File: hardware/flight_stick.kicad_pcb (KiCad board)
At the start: 2 copper layers, 75 x 50 mm, 61 parts, among them J1 Load Cell 1, J10 USB_C_Receptacle_USB2.0, J11 Conn_01x05_Pin, J3 Load Cell 2, J5 Load Cell 3, J7 Conn_01x04_Male, J8 Conn_01x05_Pin, J9 Conn_ST_STDC14, Q4 2N7002, Q5 2N7002, Q6 2N7002, Q7 2N7002, Q8 2N7002, SW1 KMR223G LFG, U1 ADS131M03IRUKx, U2 LM3940IMP-3.3/NOPB, U4 STM32F103CBU6, Y1 8M

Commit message: Finished footprint assignment and deleted pcb
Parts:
- removed C1, C16, C17, C18, C19, C2, C3, C5, C6: 100n, Capacitor_SMD:C_0603_1608Metric
- removed C20: 470n, Capacitor_SMD:C_0603_1608Metric
- removed C4: 220n, Capacitor_SMD:C_0603_1608Metric
- removed C7, C8, C9: 10u, Capacitor_SMD:C_0603_1608Metric
- removed D1, D2, D3: LED, LED_SMD:LED_0805_2012Metric
- removed D4: SMLVN6RGB, LED_SMD:LED_ROHM_SMLVN6
- removed H1, H2, H3: MountingHole, MountingHole:MountingHole_3.2mm_M3_ISO7380
- removed J1: Load Cell 1, Connector_PinHeader_1.27mm:PinHeader_1x04_P1.27mm_Vertical
- removed J10: USB_C_Receptacle_USB2.0, Connector_USB:USB_C_Receptacle_HRO_TYPE-C-31-M-12
- removed J11, J8: Conn_01x05_Pin, Connector_PinHeader_2.54mm:PinHeader_1x05_P2.54mm_Vertical
- removed J3: Load Cell 2, Connector_PinHeader_1.27mm:PinHeader_1x04_P1.27mm_Vertical
- removed J5: Load Cell 3, Connector_PinHeader_1.27mm:PinHeader_1x04_P1.27mm_Vertical
- removed J7: Conn_01x04_Male, Connector_JST:JST_XH_B4B-XH-A_1x04_P2.50mm_Vertical
- removed J9: Conn_ST_STDC14, Connector_PinHeader_1.27mm:PinHeader_2x07_P1.27mm_Vertical_SMD
- removed Q4, Q5, Q6, Q7, Q8: 2N7002, Package_TO_SOT_SMD:SOT-23
- removed R1, R2, R3, R4, R5, R6: 1k, Resistor_SMD:R_0603_1608Metric
- removed R10, R8: 50, Resistor_SMD:R_0603_1608Metric
- removed R20, R25, R26, R27, R28, R29: 10k, Resistor_SMD:R_0603_1608Metric
- removed R21, R22: 22, Resistor_SMD:R_0603_1608Metric
- removed R23, R24: 5.1K, Resistor_SMD:R_0603_1608Metric
- removed R30: 200, Resistor_SMD:R_0603_1608Metric
- removed R31: 300, Resistor_SMD:R_0603_1608Metric
- removed R7, R9: 100, Resistor_SMD:R_0603_1608Metric
- removed SW1: KMR223G LFG, flight_stick_footprints:KMR2_G_CNK
- removed U1: ADS131M03IRUKx, flight_stick_footprints:QFN_WQFN_RUK_TEX
- removed U2: LM3940IMP-3.3/NOPB, flight_stick_footprints:MP04A
- removed U4: STM32F103CBU6, Package_DFN_QFN:QFN-48-1EP_7x7mm_P0.5mm_EP5.6x5.6mm
- removed Y1: 8M, Crystal:Resonator_SMD_Murata_CSTxExxV-3Pin_3.0x1.1mm
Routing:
- net GND: track 301.4 -> 0.00 mm, vias 13 -> 0
- net +3.3V: track 190.1 -> 0.00 mm, vias 11 -> 0
- net +5V: track 102.4 -> 0.00 mm, vias 3 -> 0
- net /Trans5: track 53.9 -> 0.00 mm, vias 4 -> 0
- net /SCL: track 44.0 -> 0.00 mm
- net /SDA: track 41.7 -> 0.00 mm
- net /Trans4: track 41.1 -> 0.00 mm, vias 2 -> 0
- net /codeio: track 39.9 -> 0.00 mm, vias 4 -> 0
- net /mcureset: track 39.2 -> 0.00 mm, vias 4 -> 0
- net /Trans3: track 36.0 -> 0.00 mm, vias 2 -> 0
- net /button3: track 35.8 -> 0.00 mm, vias 1 -> 0
- net /ADC_CS: track 32.9 -> 0.00 mm, vias 2 -> 0
- net Net-(U4-PA7): track 32.5 -> 0.00 mm
- net /ADC_MCK: track 32.3 -> 0.00 mm, vias 2 -> 0
- net /ADC_SDO: track 29.7 -> 0.00 mm, vias 2 -> 0
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- removed copper zone on F.Cu, net GND
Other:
- board outline removed
- board text removed: "+"
- board text removed: "-"
- board text removed: "1 2 3 4 5"
- board text removed: "3V3"
- board text removed: "5 4 3 2 1"
- board text removed: "5V"
- board text removed: "A+"
- board text removed: "A-"
- board text removed: "Aryan Ghosh ^_^"
- board text removed: "CL"
- board text removed: "DA"
- board text removed: "University of Toronto Human Powered Vehicles Design Team"

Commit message: Began layout placement
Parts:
- added C1: 2.2u, Capacitor_SMD:C_0603_1608Metric, F.Cu at (42.2, 48.7)
- added C11: 100n, Capacitor_SMD:C_0603_1608Metric, F.Cu at (97.3, 58.7)
- added C12: 100n, Capacitor_SMD:C_0603_1608Metric, F.Cu at (97.3, 61.2)
- added C13: 220n, Capacitor_SMD:C_0603_1608Metric, F.Cu at (101.3, 53.7)
- added C14: 100n, Capacitor_SMD:C_0603_1608Metric, F.Cu at (101.3, 56.2)
- added C16: 100n, Capacitor_SMD:C_0603_1608Metric, F.Cu at (103.0, 81.0)
- added C17: 100n, Capacitor_SMD:C_0603_1608Metric, F.Cu at (103.8, 73.6)
- added C18: 100n, Capacitor_SMD:C_0603_1608Metric, F.Cu at (93.5, 81.0)
- added C19: 100n, Capacitor_SMD:C_0603_1608Metric, F.Cu at (97.0, 71.6)
- added C2: 22u, Capacitor_SMD:C_0603_1608Metric, F.Cu at (42.2, 51.2)
- added C23: 1u, Capacitor_SMD:C_0402_1005Metric, F.Cu at (11.5, 61.1)
- added C8: 100n, Capacitor_SMD:C_0603_1608Metric, F.Cu at (97.3, 53.7)
- added C9: 100n, Capacitor_SMD:C_0603_1608Metric, F.Cu at (97.3, 56.2)
- added D1: GREEN_LED, LED_SMD:LED_0805_2012Metric, F.Cu at (50.9, 58.0)
- added D10: D, Diode_SMD:D_SOD-123, F.Cu at (-1.49, 28.7)
- added D11: D, Diode_SMD:D_SOD-123, F.Cu at (-1.49, 32.0)
- added D12: D, Diode_SMD:D_SOD-123, F.Cu at (-1.49, 35.4)
- added D13: D, Diode_SMD:D_SOD-123, F.Cu at (4.30, 15.3)
- added D14: D, Diode_SMD:D_SOD-123, F.Cu at (4.30, 18.6)
- added D15: D, Diode_SMD:D_SOD-123, F.Cu at (4.30, 22.0)
- added D16: D, Diode_SMD:D_SOD-123, F.Cu at (4.30, 25.3)
- added D17: D, Diode_SMD:D_SOD-123, F.Cu at (4.30, 28.7)
- added D18: D, Diode_SMD:D_SOD-123, F.Cu at (4.30, 32.0)
- added D19: D, Diode_SMD:D_SOD-123, F.Cu at (4.30, 35.4)
- added D20: D, Diode_SMD:D_SOD-123, F.Cu at (10.1, 15.3)
- added D21: D, Diode_SMD:D_SOD-123, F.Cu at (10.1, 18.6)
- added D22: D, Diode_SMD:D_SOD-123, F.Cu at (10.1, 22.0)
- added D23: D, Diode_SMD:D_SOD-123, F.Cu at (10.1, 25.3)
- added D24: D, Diode_SMD:D_SOD-123, F.Cu at (10.1, 28.7)
- added D25: D, Diode_SMD:D_SOD-123, F.Cu at (10.1, 32.0)
- added D26: D, Diode_SMD:D_SOD-123, F.Cu at (10.1, 35.4)
- added D27: D, Diode_SMD:D_SOD-123, F.Cu at (15.9, 15.3)
- added D28: D, Diode_SMD:D_SOD-123, F.Cu at (15.9, 18.6)
- added D29: D, Diode_SMD:D_SOD-123, F.Cu at (15.9, 22.0)
- added D3: D, Diode_SMD:D_SOD-123, F.Cu at (-1.49, 15.3)
- added D30: D, Diode_SMD:D_SOD-123, F.Cu at (15.9, 25.3)
- added D4: SMLVN6RGB, LED_SMD:LED_ROHM_SMLVN6, F.Cu at (33.5, 43.0)
- added D5: D, Diode_SMD:D_SOD-123, F.Cu at (-1.49, 18.6)
- added D6: SS34, Diode_SMD:D_SMA, F.Cu at (48.2, 49.7)
- added D7: SS34, Diode_SMD:D_SMA, F.Cu at (48.2, 54.2)
- added D8: D, Diode_SMD:D_SOD-123, F.Cu at (-1.49, 22.0)
- added D9: D, Diode_SMD:D_SOD-123, F.Cu at (-1.49, 25.3)
- added J1: Conn_01x04_Male, Connector_JST:JST_XH_B4B-XH-A_1x04_P2.50mm_Vertical, F.Cu at (-0.94, 58.9)
- added J10: USB_C_Receptacle_USB2.0, Connector_USB:USB_C_Receptacle_HRO_TYPE-C-31-M-12, F.Cu at (105.8, 91.5)
- added J12: Load Cell 2, Connector_PinHeader_1.27mm:PinHeader_1x04_P1.27mm_Vertical, F.Cu at (105.7, 47.0)
- added J2: Conn_02x05_Top_Bottom, Connector_JST:JST_J2100_B10B-J21DK-GGXR_2x05_P2.50x4.00mm_Vertical, F.Cu at (24.9, 19.1)
- added J3: Conn_01x04_Male, Connector_JST:JST_XH_B4B-XH-A_1x04_P2.50mm_Vertical, F.Cu at (-0.94, 66.7)
- added J4: Load Cell 3, Connector_PinHeader_1.27mm:PinHeader_1x04_P1.27mm_Vertical, F.Cu at (97.3, 47.0)
- added J6: Load Cell 1, Connector_PinHeader_1.27mm:PinHeader_1x04_P1.27mm_Vertical, F.Cu at (101.5, 47.0)
- added J7: Conn_02x05_Top_Bottom, Connector_JST:JST_J2100_B10B-J21DK-GGXR_2x05_P2.50x4.00mm_Vertical, F.Cu at (-0.25, 42.5)
- added J9: Conn_ST_STDC14, Connector_PinHeader_1.27mm:PinHeader_2x07_P1.27mm_Vertical_SMD, F.Cu at (85.0, 84.3)
- added L2: 10uH, Inductor_SMD:L_0603_1608Metric, F.Cu at (42.2, 53.7)
- added R1: 10k, Resistor_SMD:R_0603_1608Metric, F.Cu at (42.2, 56.2)
- added R10: 200, Resistor_SMD:R_0603_1608Metric, F.Cu at (44.6, 24.9)
- added R12: 1k, Resistor_SMD:R_0603_1608Metric, F.Cu at (101.3, 58.7)
- added R13: 1k, Resistor_SMD:R_0603_1608Metric, F.Cu at (101.3, 61.2)
- added R14: 1k, Resistor_SMD:R_0603_1608Metric, F.Cu at (105.3, 53.7)
- added R15: 1k, Resistor_SMD:R_0603_1608Metric, F.Cu at (105.3, 56.2)
- added R16: 1k, Resistor_SMD:R_0603_1608Metric, F.Cu at (105.3, 58.7)
- added R17: 1k, Resistor_SMD:R_0603_1608Metric, F.Cu at (105.3, 61.2)
- added R2: 4.7k, Resistor_SMD:R_0603_1608Metric, F.Cu at (108.3, 72.9)
- added R20: 10k, Resistor_SMD:R_0603_1608Metric, F.Cu at (97.0, 70.0)
- added R23: 5.1K, Resistor_SMD:R_0603_1608Metric, F.Cu at (99.5, 88.5)
- added R24: 5.1K, Resistor_SMD:R_0603_1608Metric, F.Cu at (112.5, 88.5)
- added R3: 4.7k, Resistor_SMD:R_0603_1608Metric, F.Cu at (112.3, 62.9)
- added R30: 10k, Resistor_SMD:R_0603_1608Metric, F.Cu at (15.4, 40.8)
- added R31: 10k, Resistor_SMD:R_0603_1608Metric, F.Cu at (15.4, 43.3)
- added R32: 10k, Resistor_SMD:R_0603_1608Metric, F.Cu at (15.4, 45.8)
- added R33: 10k, Resistor_SMD:R_0603_1608Metric, F.Cu at (15.4, 48.3)
- added R4: 400, Resistor_SMD:R_0603_1608Metric, F.Cu at (42.2, 58.7)
- added R5: 10k, Resistor_SMD:R_0603_1608Metric, F.Cu at (15.4, 38.3)
- added R7: 1.5k, Resistor_SMD:R_0603_1608Metric, F.Cu at (106.5, 83.8)
- added R8: 200, Resistor_SMD:R_0603_1608Metric, F.Cu at (44.6, 19.9)
- added R9: 200, Resistor_SMD:R_0603_1608Metric, F.Cu at (44.6, 22.4)
- added SW1: KMR223G LFG, flight_stick_footprints:KMR2_G_CNK, F.Cu at (93.0, 69.5)
- added U1: TPS62175DQC, Package_SON:WSON-10-1EP_2x3mm_P0.5mm_EP0.84x2.4mm_ThermalVias, F.Cu at (46.5, 58.8)
- added U2: AT24CS01-MAHM, Package_DFN_QFN:DFN-8-1EP_3x2mm_P0.5mm_EP1.3x1.5mm, F.Cu at (109.2, 76.1)
- added U3: ADS131M03IRUKx, flight_stick_footprints:QFN_WQFN_RUK_TEX, F.Cu at (35.5, 57.4)
- added U4: STM32F103CBU6, Package_DFN_QFN:QFN-48-1EP_7x7mm_P0.5mm_EP5.6x5.6mm, F.Cu at (98.5, 76.5)
- added U5: USBLC6-2SC6, Package_TO_SOT_SMD:SOT-23-6, F.Cu at (100.0, 84.0)
- added U6: TCAN3403, Package_TO_SOT_SMD:TSOT-23-8, F.Cu at (12.6, 57.9)
- added Y1: 8M, Crystal:Resonator_SMD_Murata_CSTxExxV-3Pin_3.0x1.1mm, F.Cu at (100.8, 70.6)

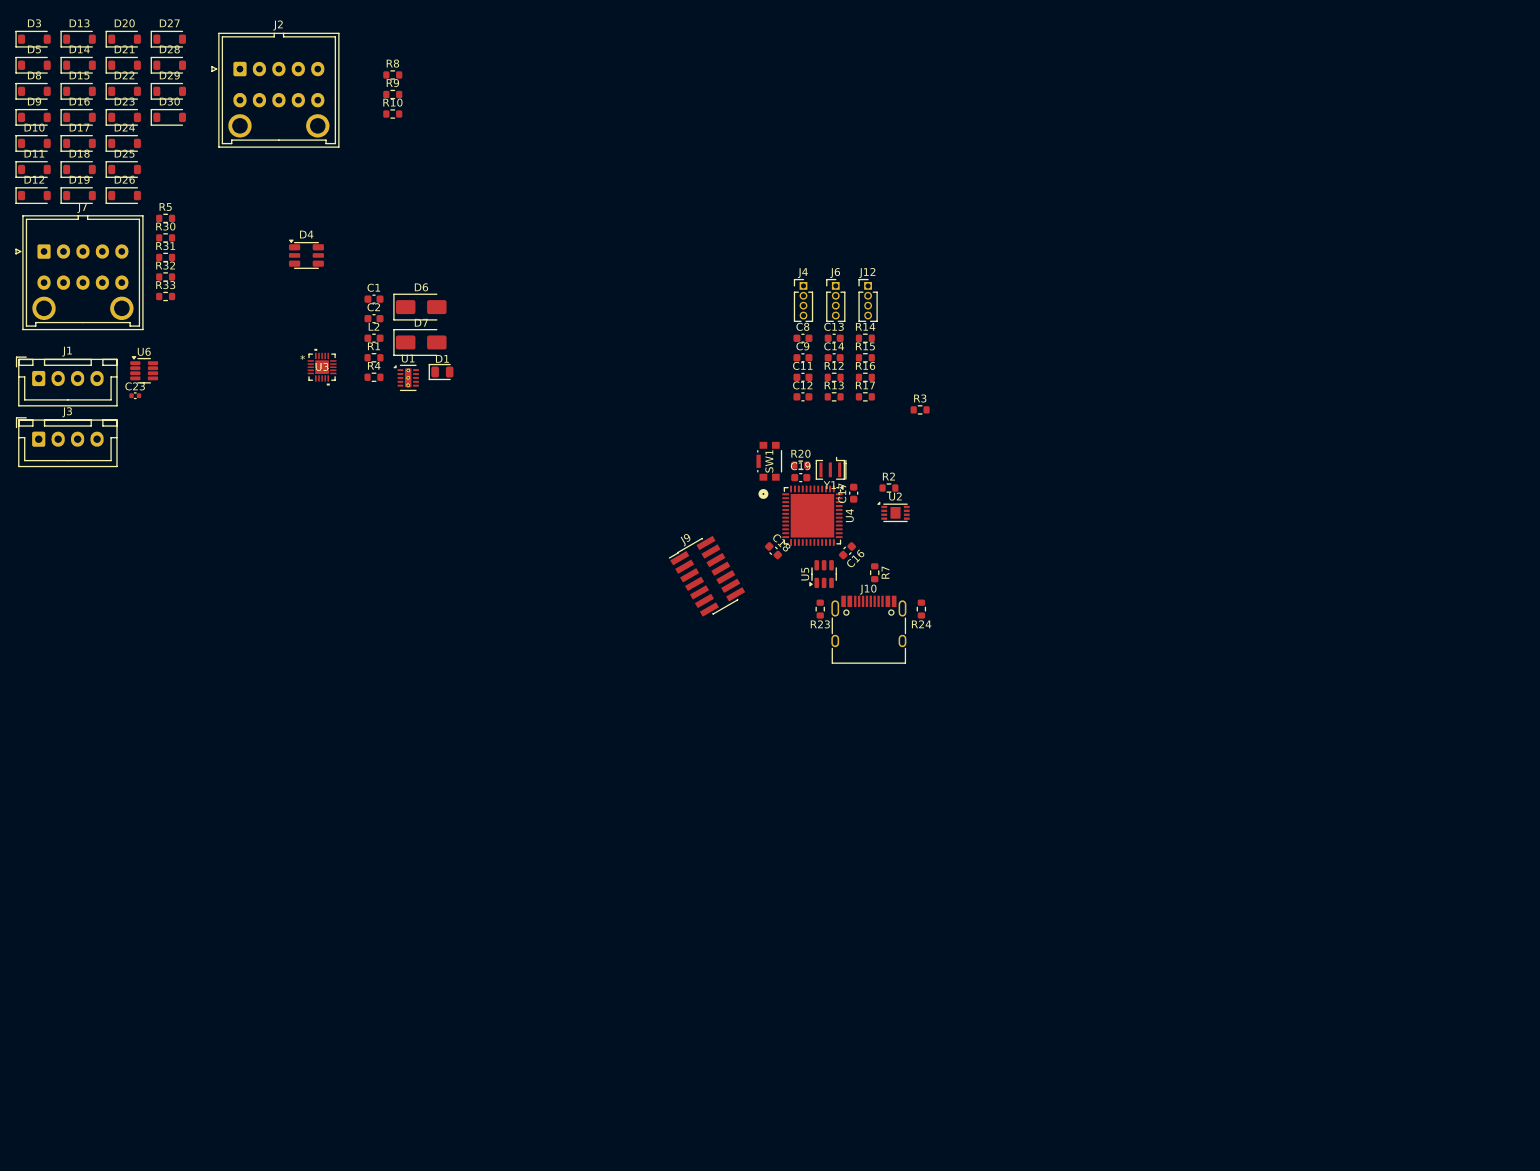
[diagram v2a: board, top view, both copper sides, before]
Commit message: modified mcu pin alloc and pre-routing placement
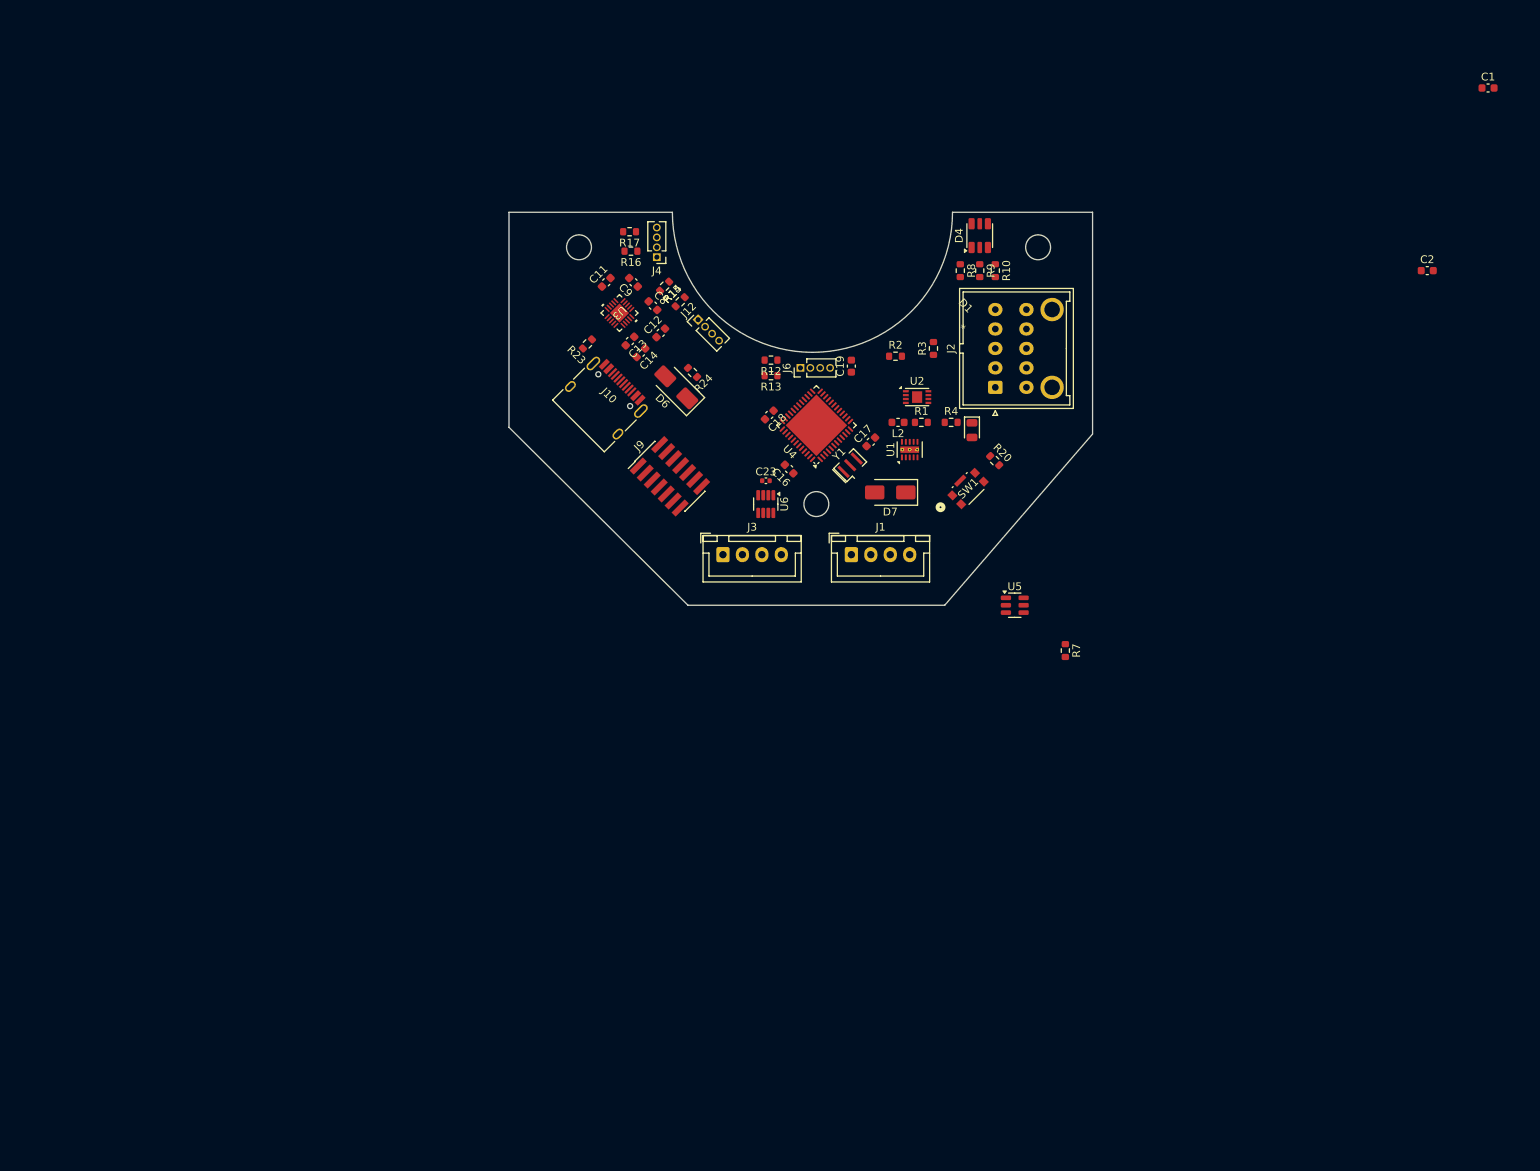
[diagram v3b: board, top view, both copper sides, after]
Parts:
- removed D10, D11, D12, D13, D14, D15, D16, D17, D18, D19, D20, D21, D22, D23, D24, D25, D26, D27, D28, D29, D3, D30, D5, D8, D9: D, Diode_SMD:D_SOD-123
- removed J7: Conn_02x05_Top_Bottom, Connector_JST:JST_J2100_B10B-J21DK-GGXR_2x05_P2.50x4.00mm_Vertical
- removed R30, R31, R32, R33, R5: 10k, Resistor_SMD:R_0603_1608Metric
- added H1: MountingHole, MountingHole:MountingHole_3.2mm_M3, F.Cu at (68.5, 42.0)
- added H2: MountingHole, MountingHole:MountingHole_3.2mm_M3, F.Cu at (127.5, 42.0)
- added H3: MountingHole, MountingHole:MountingHole_3.2mm_M3, F.Cu at (99.0, 75.0)
- moved C1 145.7 mm to (185.3, 21.5)
- moved C2 135.5 mm to (177.5, 45.0)
- moved J1 106.9 mm to (103.5, 81.5)
- moved J2 105.3 mm to (122.0, 60.0), turned to 90 degrees
- moved J3 89.2 mm to (87.0, 81.5)
- moved D4 86.6 mm to (120.0, 40.5), turned to 90 degrees
- moved C23 81.8 mm to (92.5, 72.0)
- moved U6 81.7 mm to (92.5, 75.0), turned to -90 degrees
- moved R10 80.0 mm to (122.0, 45.0), turned to -90 degrees
- moved R9 78.8 mm to (120.0, 45.0), turned to -90 degrees
- moved R8 77.1 mm to (117.5, 45.0), turned to -90 degrees
- moved R4 74.4 mm to (116.3, 64.5)
- moved R1 70.8 mm to (112.5, 64.5)
- moved D1 68.5 mm to (119.0, 65.5), turned to -90 degrees
- moved L2 68.2 mm to (109.5, 64.5), turned to 180 degrees
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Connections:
- U4 pad 12: /COMPRT_TX -> /MTX_COL2
- U4 pad 13: /COMPRT_RX -> /MTX_COL3
- U4 pad 14: /MTX_COL2 -> /MTX_COL4
- U4 pad 15: /MTX_COL3 -> /MTX_COL5
- U4 pad 16: /MTX_COL4 -> /MTX_ROW1
- U4 pad 17: /MTX_COL5 -> /MTX_ROW2
- U4 pad 18: /MTX_ROW1 -> /MTX_ROW3
- U4 pad 19: /MTX_ROW2 -> /MTX_ROW4
- U4 pad 20: /MTX_ROW3 -> /MTX_ROW5
- U4 pad 21: /MTX_ROW4 -> /ADC_CS
- U4 pad 22: /MTX_ROW5 -> /ADC_RST
- U4 pad 30: /ADC_CS -> /COMPRT_TX
- U4 pad 31: /ADC_RST -> /COMPRT_RX
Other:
- board outline added: 75 x 50.5 mm
- board text added: "1 in. Shaft Outer Diameter"

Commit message: Completed first layout draft
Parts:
- added C3: 2.2u, Capacitor_SMD:C_0603_1608Metric, F.Cu at (102.0, 86.5)
- added NT1: NetTie_2, NetTie:NetTie-2_THT_Pad1.0mm, F.Cu at (71.5, 57.7)
- J2: value Conn_02x05_Top_Bottom -> Conn_02x05_Odd_Even; footprint Connector_JST:JST_J2100_B10B-J21DK-GGXR_2x05_P2.50x4.00mm_Vertical -> Connector_JST:JST_PUD_B10B-PUDSS_2x05_P2.00mm_Vertical
- R1: value 10k -> 100k
- moved C1 110.9 mm to (95.5, 86.5), turned to 90 degrees
- moved C2 84.1 mm to (102.0, 82.0), turned to -90 degrees
- moved R7 60.1 mm to (77.0, 67.5), turned to 135 degrees
- moved U5 47.2 mm to (82.5, 66.5)
- moved R20 38.7 mm to (85.5, 82.5)
- moved SW1 37.5 mm to (83.0, 85.0), turned to -45 degrees
- moved D6 28.2 mm to (90.5, 86.5), turned to 180 degrees
- moved J3 27.7 mm to (114.7, 82.8), turned to 45 degrees
- moved J1 23.9 mm to (125.5, 72.0), turned to 45 degrees
- moved L2 22.8 mm to (95.5, 82.5), turned to -90 degrees
- moved R1 22.0 mm to (98.5, 81.5)
- moved U1 20.8 mm to (99.0, 85.0)
- moved U6 20.0 mm to (112.5, 76.0), turned to -45 degrees
- moved D1 19.4 mm to (108.0, 81.5), turned to 180 degrees
- moved R4 18.7 mm to (104.5, 79.0)
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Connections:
- net Net-(U4-PD0) renamed /OSC+
- net Net-(U4-PD1) renamed /OSC-
- C12 pad 2: GND -> GNDA
- J12 pad 4: GND -> GNDA
- J2 pad 2: /MTX_ROW2 -> /MTX_COL1
- J2 pad 3: /MTX_ROW3 -> /MTX_ROW2
- J2 pad 4: /MTX_ROW4 -> /MTX_COL2
- J2 pad 5: /MTX_ROW5 -> /MTX_ROW3
- J2 pad 6: /MTX_COL1 -> /MTX_COL3
- J2 pad 7: /MTX_COL2 -> /MTX_ROW4
- J2 pad 8: /MTX_COL3 -> /MTX_COL4
- J2 pad 9: /MTX_COL4 -> /MTX_ROW5
- J4 pad 4: GND -> GNDA
- J6 pad 4: GND -> GNDA
- R4 pad 1: /Power/PG -> +3.3V
- U3 pad 20: GND -> GNDA
- U3 pad 21: GND -> GNDA
- U4 pad 11: /MTX_COL1 -> /MTX_COL5
- U4 pad 12: /MTX_COL2 -> /MTX_COL4
- U4 pad 14: /MTX_COL4 -> /MTX_COL2
- U4 pad 15: /MTX_COL5 -> /MTX_COL1
- U4 pad 21: /ADC_CS -> /EEPROM_SCK
- U4 pad 22: /ADC_RST -> /EEPROM_SDA
- U4 pad 30: /COMPRT_TX -> /ADC_CS
- U4 pad 31: /COMPRT_RX -> /ADC_RST
- U4 pad 42: /EEPROM_SCK -> /COMPRT_TX
- U4 pad 43: /EEPROM_SDA -> /COMPRT_RX
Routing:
- net GND: track 0.00 -> 175.7 mm, vias 0 -> 8
- net +3.3V: track 0.00 -> 102.9 mm, vias 0 -> 9
- net +5V: track 0.00 -> 60.1 mm, vias 0 -> 2
- net /RESET: track 0.00 -> 55.7 mm, vias 0 -> 3
- net /MTX_COL5: track 0.00 -> 45.0 mm
- net /MTX_COL4: track 0.00 -> 41.5 mm
- net /RGB_B: track 0.00 -> 40.9 mm, vias 0 -> 2
- net /RGB_G: track 0.00 -> 39.3 mm, vias 0 -> 2
- net /RGB_R: track 0.00 -> 39.2 mm, vias 0 -> 2
- net /MTX_COL3: track 0.00 -> 38.3 mm
- net /MTX_COL2: track 0.00 -> 35.8 mm
- net /MTX_ROW5: track 0.00 -> 34.8 mm
- net /ADC_DRDY: track 0.00 -> 34.3 mm, vias 0 -> 2
- net /MTX_ROW4: track 0.00 -> 33.8 mm
- net /MTX_ROW3: track 0.00 -> 32.8 mm
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- added copper zone on In1.Cu, net +3.3V
- added copper zone on In2.Cu, net GND
- added copper zone on In2.Cu, net GNDA
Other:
- board size 75 x 50.5 mm -> 76 x 51.5 mm
- copper layers 2 -> 4
